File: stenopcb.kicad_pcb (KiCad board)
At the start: 2 copper layers, 97.8 x 97.8 mm, 85 parts, among them K1 MAIN_RIGHT_TO_VOWELS_RIGHT, K2 MAIN_LEFT_TO_VOWELS_LEFT, K3 VOWELS_RIGHT_IN, K4 VOWELS_LEFT_IN, P1 MAIN_RIGHT_IN, P2 MAIN_RIGHT_TO_MAIN_LEFT, P3 MAIN_LEFT_IN, SW1 SPST, SW10 SPST, SW11 SPST, SW12 SPST, SW13 SPST, SW14 SPST, SW15 SPST, SW16 SPST, SW17 SPST, SW18 SPST, SW19 SPST, SW2 SPST, SW20 SPST, SW21 SPST, SW22 SPST, SW23 SPST, SW24 SPST, SW25 SPST, SW26 SPST, SW27 SPST, SW28 SPST, SW29 SPST, SW3 SPST, SW30 SPST, SW4 SPST, SW5 SPST, SW6 SPST, SW7 SPST, SW8 SPST, SW9 SPST

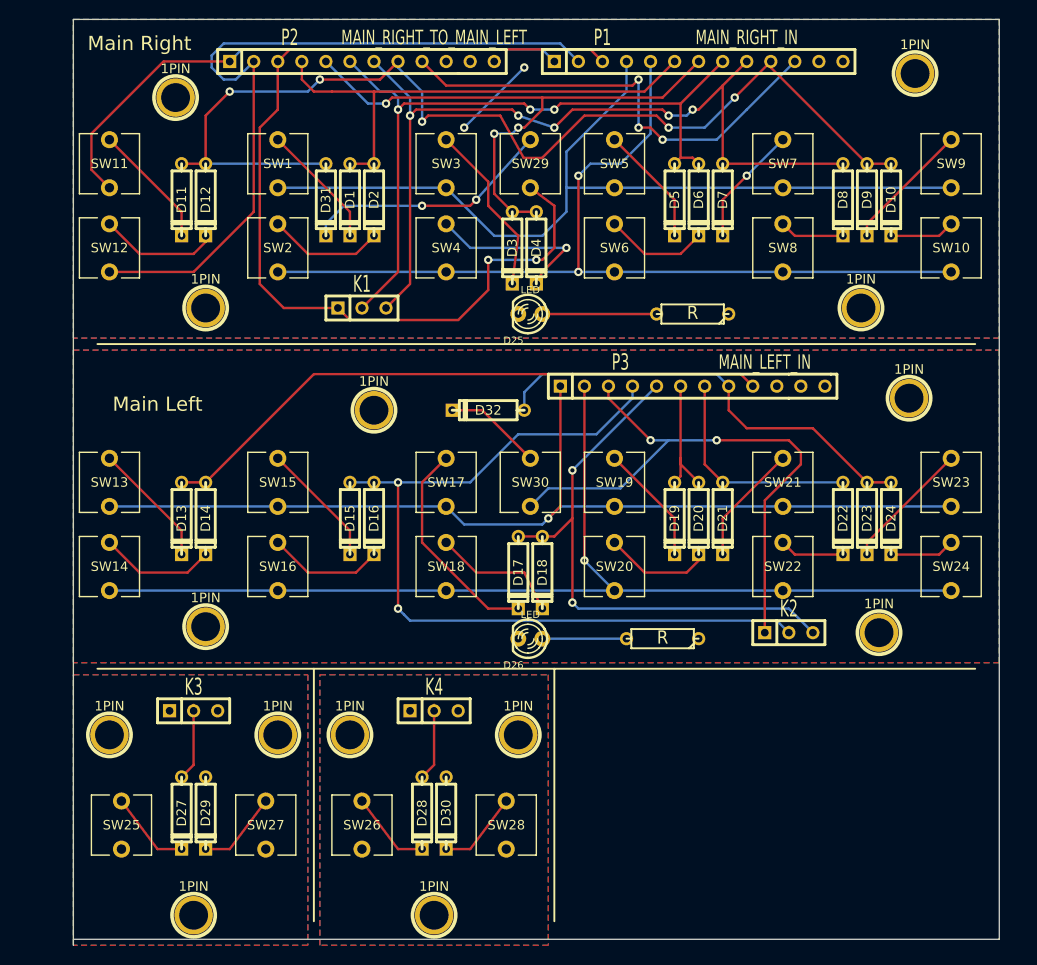
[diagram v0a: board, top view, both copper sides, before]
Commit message: fixed 3-pin connector on main right, and made vowel boards smaller
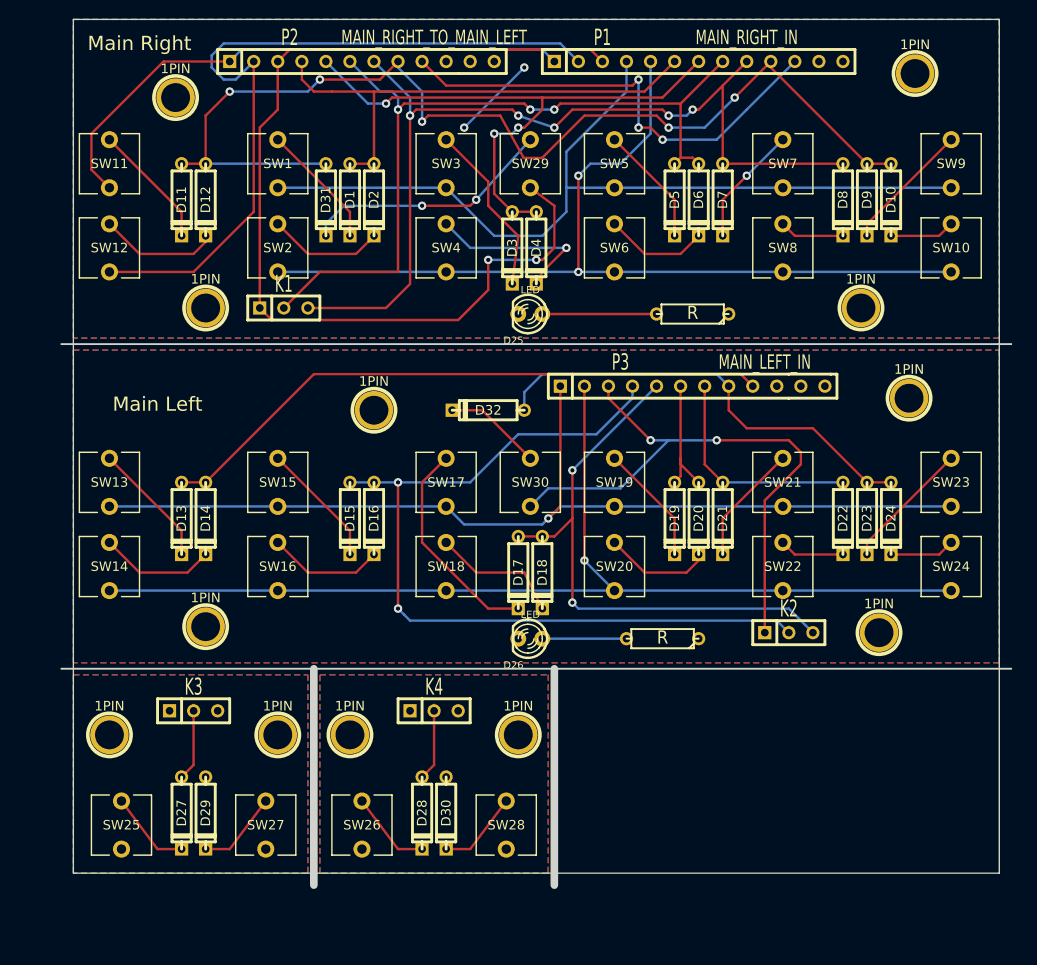
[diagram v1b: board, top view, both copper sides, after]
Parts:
- removed the 1PIN at (123.8, 156.8)
- removed the 1PIN at (149.2, 156.8)
- moved K1 8.25 mm to (133.3, 92.7)
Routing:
- net /COL_3: track 89.3 -> 97.6 mm
- net /COL_2: track 76.2 -> 84.4 mm
- net /ROW_2: track 105.0 -> 106.4 mm
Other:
- board size 97.8 x 97.8 mm -> 100.3 x 91.4 mm
- board text added: "Routing"
- board text added: "V-Scoring"

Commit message: added information text on silkscreen
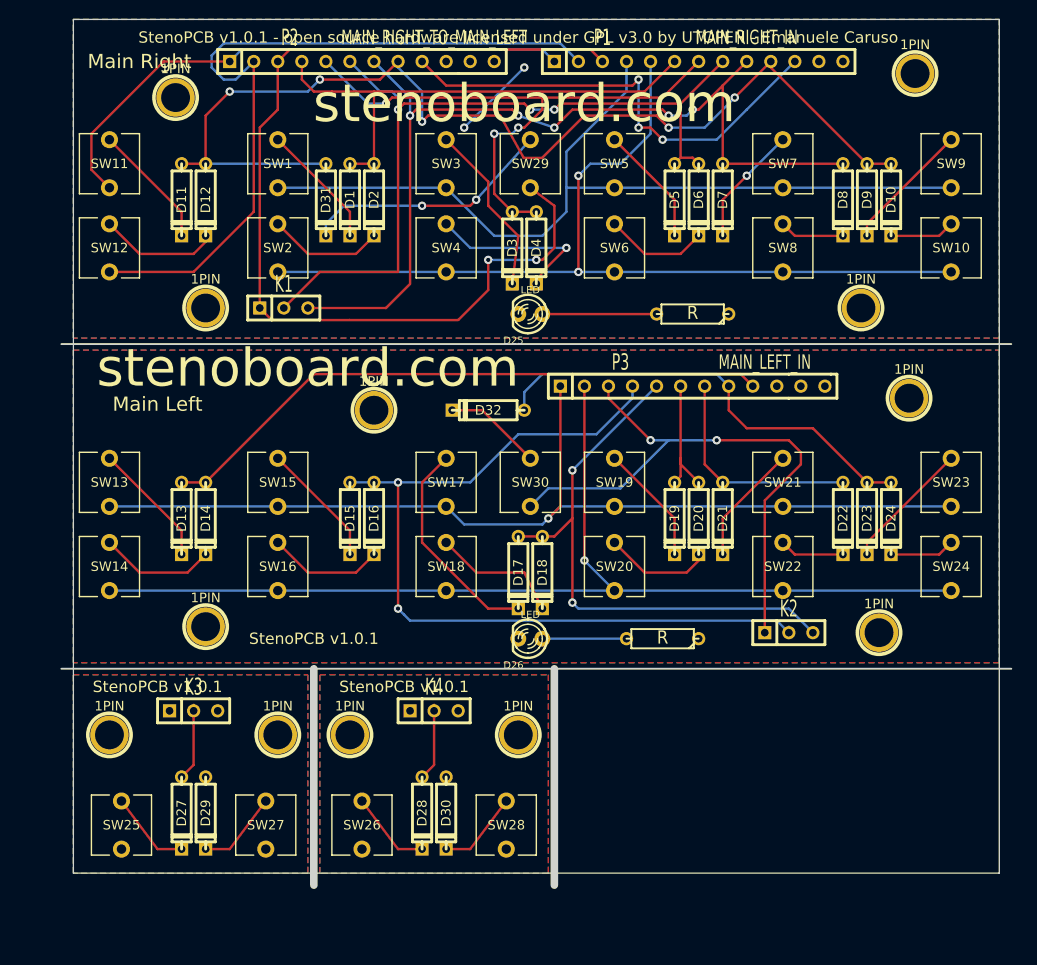
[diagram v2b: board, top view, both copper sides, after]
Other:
- board text added: "StenoPCB v1.0.1"
- board text added: "StenoPCB v1.0.1 - open source hardware licensed under GPL v3.0 by UTOPEN - Emanuele Caruso"
- board text added: "stenoboard.com"
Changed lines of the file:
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@@
     (area 91.694999 45.410001 231.440714 177.325)
     (thickness 1.6)
-    (drawings 36)
+    (drawings 42)
     (tracks 346)
     (zones 0)
@@
     )
   )
+  (gr_text "StenoPCB v1.0.1" (at 120.015 132.715) (layer F.SilkS)
+    (effects (font (size 1.2 1.2) (thickness 0.3)))
+  )
+  (gr_text "StenoPCB v1.0.1" (at 146.05 132.715) (layer F.SilkS)
+    (effects (font (size 1.2 1.2) (thickness 0.3)))
+  )
+  (gr_text "StenoPCB v1.0.1" (at 136.525 127.635) (layer F.SilkS)
+    (effects (font (size 1.2 1.2) (thickness 0.3)))
+  )
+  (gr_text "StenoPCB v1.0.1 - open source hardware licensed under GPL v3.0 by UTOPEN - Emanuele Caruso" (at 158.115 64.135) (layer F.SilkS)
+    (effects (font (size 1.2 1.2) (thickness 0.3)))
+  )
+  (gr_text stenoboard.com (at 135.89 99.06) (layer F.SilkS)
+    (effects (font (size 4 4) (thickness 0.3)))
+  )
+  (gr_text stenoboard.com (at 158.75 71.12) (layer F.SilkS)
+    (effects (font (size 4 4) (thickness 0.3)))
+  )
   (gr_line (start 161.925 130.81) (end 161.925 153.67) (angle 90) (layer Edge.Cuts) (width 0.8))
   (gr_line (start 136.525 130.81) (end 136.525 153.67) (angle 90) (layer Edge.Cuts) (width 0.8))
@@
     (effects (font (size 1.5 1.5) (thickness 0.3)))
   )
-  (gr_text "Main Right" (at 118.11 64.77) (layer F.SilkS)
+  (gr_text "Main Right" (at 118.11 66.675) (layer F.SilkS)
     (effects (font (size 1.5 1.5) (thickness 0.3)))
   )

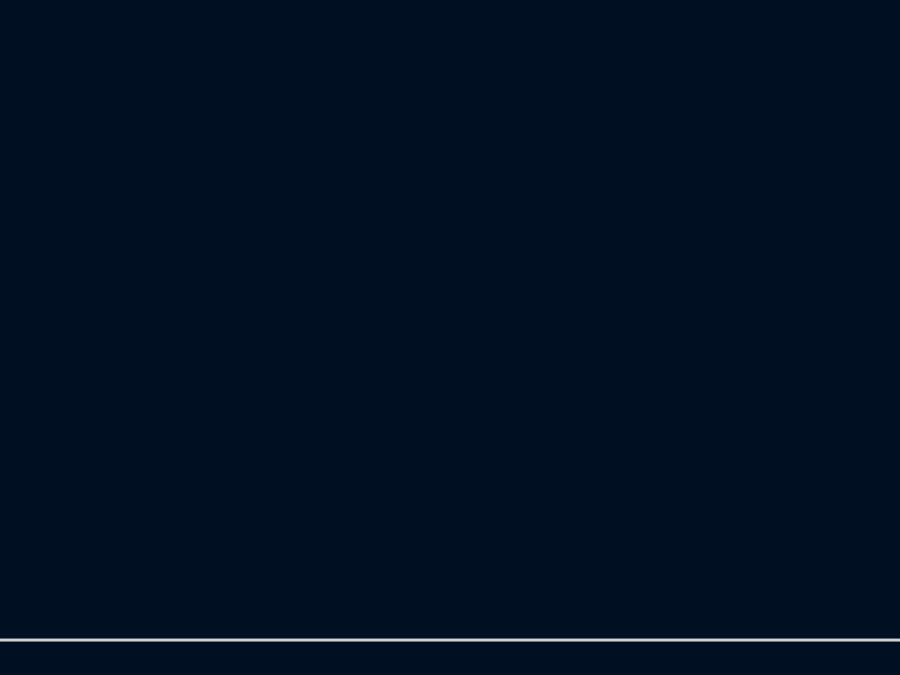
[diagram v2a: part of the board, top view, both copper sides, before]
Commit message: added TOP and BOT copper layers labels
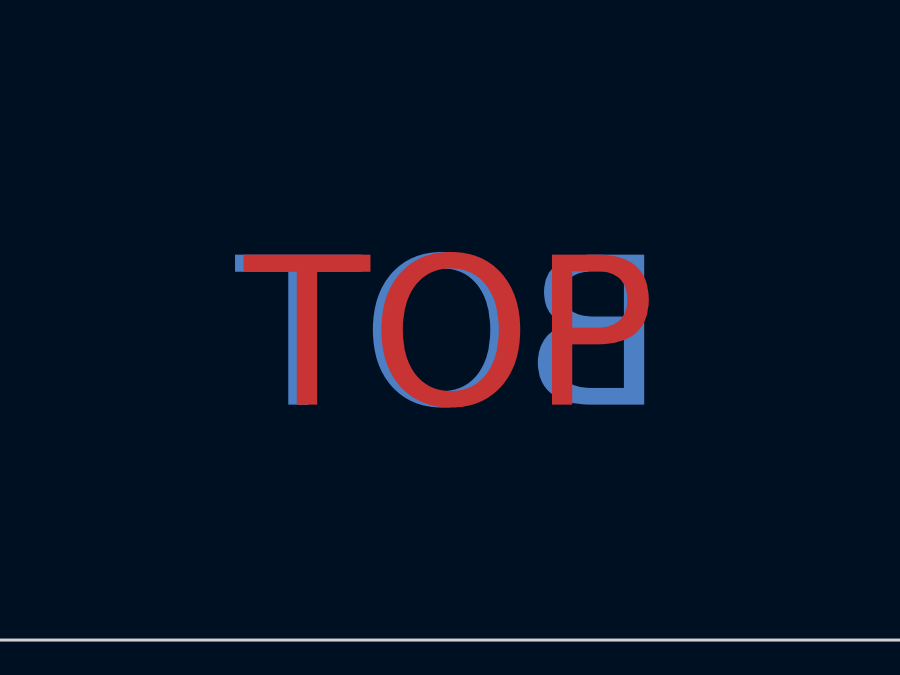
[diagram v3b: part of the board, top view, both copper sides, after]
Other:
- board text added: "BOT"
- board text added: "TOP"
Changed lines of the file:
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@@
     (area 91.694999 45.410001 231.440714 177.325)
     (thickness 1.6)
-    (drawings 42)
+    (drawings 44)
     (tracks 346)
     (zones 0)
@@
     )
   )
+  (gr_text BOT (at 186.055 142.24) (layer B.Cu)
+    (effects (font (size 5 5) (thickness 0.3)) (justify mirror))
+  )
+  (gr_text TOP (at 186.055 142.24) (layer F.Cu)
+    (effects (font (size 5 5) (thickness 0.3)))
+  )
   (gr_text "StenoPCB v1.0.1" (at 120.015 132.715) (layer F.SilkS)

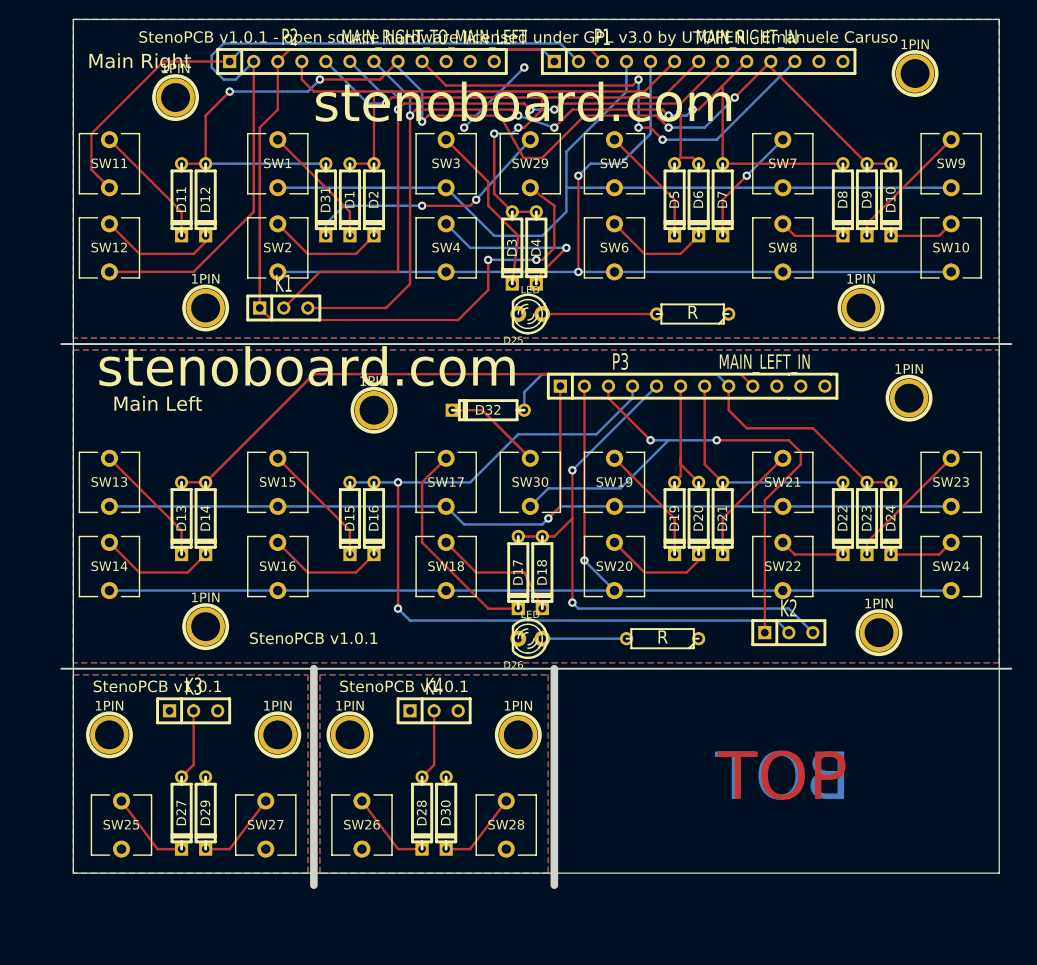
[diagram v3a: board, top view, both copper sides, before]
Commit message: added bottom margin
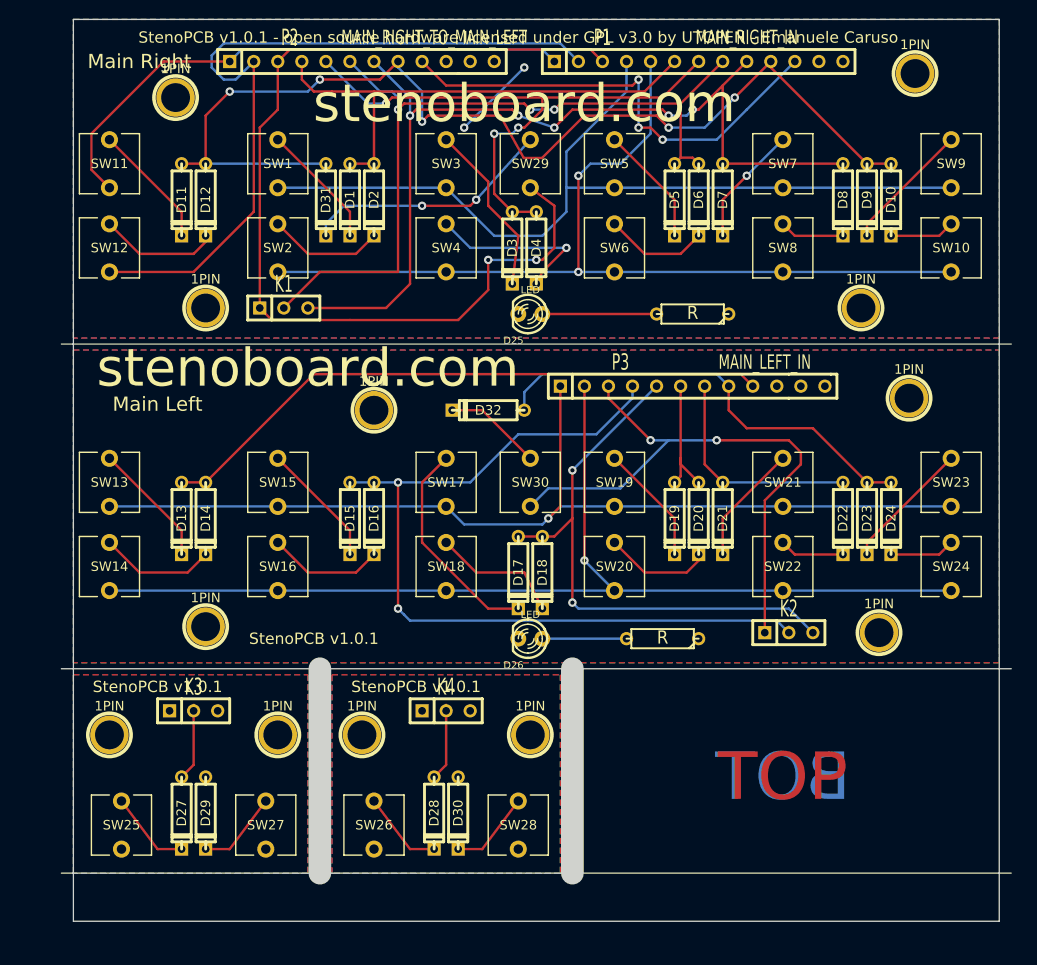
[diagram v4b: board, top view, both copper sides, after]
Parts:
- moved K4 1.27 mm to (150.5, 135.3)
- moved SW26 1.27 mm to (142.9, 147.3)
- moved SW28 1.27 mm to (158.1, 147.3)
- moved 1PIN 1.27 mm to (141.6, 137.8)
- moved 1PIN 1.27 mm to (159.4, 137.8)
- moved D28 1.27 mm to (149.2, 146.1)
- moved D30 1.27 mm to (151.8, 146.1)
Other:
- board size 100.3 x 91.4 mm -> 100.3 x 95.2 mm
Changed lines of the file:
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@@
     (area 91.694999 45.410001 231.440714 177.325)
     (thickness 1.6)
-    (drawings 44)
+    (drawings 48)
     (tracks 346)
     (zones 0)
@@
     (22 B.Mask user)
     (23 F.Mask user)
-    (24 Dwgs.User user)
+    (24 Dwgs.User user hide)
     (25 Cmts.User user)
     (26 Eco1.User user)
@@
   )
   (module SIL-3 (layer F.Cu)
-    (at 149.225 135.255)
+    (at 150.495 135.255)
     (descr "Connecteur 3 pins")
     (tags "CONN DEV")
@@
   )
   (module EVQ-P0E07K (layer F.Cu)
-    (at 156.845 147.32)
+    (at 158.115 147.32)
     (fp_text reference SW28 (at 0 0) (layer F.SilkS)
       (effects (font (size 1 1) (thickness 0.15)))
@@
   )
   (module EVQ-P0E07K (layer F.Cu)
-    (at 141.605 147.32)
+    (at 142.875 147.32)
     (fp_text reference SW26 (at 0 0) (layer F.SilkS)
       (effects (font (size 1 1) (thickness 0.15)))
@@
   )
   (module D3 (layer F.Cu)
-    (at 150.495 146.05 270)
+    (at 151.765 146.05 270)
     (descr "Diode 3 pas")
     (tags "DIODE DEV")
@@
   )
   (module D3 (layer F.Cu)
-    (at 147.955 146.05 270)
+    (at 149.225 146.05 270)
     (descr "Diode 3 pas")
     (tags "DIODE DEV")
@@
   )
   (module 1pin (layer F.Cu)
-    (at 140.335 137.795)
+    (at 141.605 137.795)
     (descr "module 1 pin (ou trou mecanique de percage)")
     (tags DEV)
@@
   )
   (module 1pin (layer F.Cu)
-    (at 158.115 137.795)
+    (at 159.385 137.795)
     (descr "module 1 pin (ou trou mecanique de percage)")
     (tags DEV)
@@
     )
   )
+  (gr_line (start 163.83 130.81) (end 163.83 152.4) (angle 90) (layer Edge.Cuts) (width 2.4))
+  (gr_line (start 137.16 130.81) (end 137.16 152.4) (angle 90) (layer Edge.Cuts) (width 2.4))
+  (gr_text V-Scoring (at 217.17 152.4) (layer Dwgs.User)
+    (effects (font (size 1.5 1.5) (thickness 0.3)))
+  )
+  (gr_line (start 109.855 152.4) (end 210.185 152.4) (angle 90) (layer Edge.Cuts) (width 0.01))
+  (gr_line (start 208.915 157.48) (end 208.915 152.4) (angle 90) (layer Edge.Cuts) (width 0.1))
+  (gr_line (start 111.125 157.48) (end 208.915 157.48) (angle 90) (layer Edge.Cuts) (width 0.1))
+  (gr_line (start 111.125 152.4) (end 111.125 157.48) (angle 90) (layer Edge.Cuts) (width 0.1))
   (gr_text BOT (at 186.055 142.24) (layer B.Cu)
     (effects (font (size 5 5) (thickness 0.3)) (justify mirror))
@@
     (effects (font (size 1.2 1.2) (thickness 0.3)))
   )
-  (gr_text "StenoPCB v1.0.1" (at 146.05 132.715) (layer F.SilkS)
+  (gr_text "StenoPCB v1.0.1" (at 147.32 132.715) (layer F.SilkS)
     (effects (font (size 1.2 1.2) (thickness 0.3)))
   )
@@
     (effects (font (size 4 4) (thickness 0.3)))
   )
-  (gr_line (start 161.925 130.81) (end 161.925 153.67) (angle 90) (layer Edge.Cuts) (width 0.8))
-  (gr_line (start 136.525 130.81) (end 136.525 153.67) (angle 90) (layer Edge.Cuts) (width 0.8))
-  (gr_text Routing (at 166.37 154.94) (layer Dwgs.User)
+  (gr_text Routing (at 167.64 156.21) (layer Dwgs.User)
     (effects (font (size 1.5 1.5) (thickness 0.3)))
   )
-  (gr_text Routing (at 140.97 154.94) (layer Dwgs.User)
+  (gr_text Routing (at 140.97 156.21) (layer Dwgs.User)
     (effects (font (size 1.5 1.5) (thickness 0.3)))
   )
@@
     (arrow2b (pts (xy 99.694998 62.23) (xy 100.281418 63.356503)))
   )
-  (gr_line (start 109.855 130.81) (end 210.185 130.81) (angle 90) (layer Edge.Cuts) (width 0.2))
-  (gr_line (start 109.855 96.52) (end 210.185 96.52) (angle 90) (layer Edge.Cuts) (width 0.2))
+  (gr_line (start 109.855 130.81) (end 210.185 130.81) (angle 90) (layer Edge.Cuts) (width 0.01))
+  (gr_line (start 109.855 96.52) (end 210.185 96.52) (angle 90) (layer Edge.Cuts) (width 0.01))
   (dimension 1.905 (width 0.3) (layer Dwgs.User)
     (gr_text "1,905 mm" (at 174.704999 151.4475 270) (layer Dwgs.User)
@@
   )
   (gr_line (start 111.125 152.4) (end 111.125 62.23) (angle 90) (layer Edge.Cuts) (width 0.1))
-  (gr_line (start 208.915 152.4) (end 111.125 152.4) (angle 90) (layer Edge.Cuts) (width 0.1))
   (gr_line (start 111.125 62.23) (end 208.915 62.23) (angle 90) (layer Edge.Cuts) (width 0.1))
   (via (at 152.4 73.66) (size 0.889) (layers F.Cu B.Cu) (net 0))
@@
   (segment (start 164.465 88.9) (end 168.275 88.9) (width 0.254) (layer B.Cu) (net 24))
   (segment (start 132.715 88.9) (end 150.495 88.9) (width 0.254) (layer B.Cu) (net 24))
-  (segment (start 149.225 134.62) (end 149.225 140.97) (width 0.254) (layer F.Cu) (net 25) (status 10))
-  (segment (start 149.225 140.97) (end 147.955 142.24) (width 0.254) (layer F.Cu) (net 25))
+  (segment (start 150.495 134.62) (end 150.495 140.97) (width 0.254) (layer F.Cu) (net 25) (status 10))
+  (segment (start 150.495 140.97) (end 149.225 142.24) (width 0.254) (layer F.Cu) (net 25))
   (segment (start 123.825 134.62) (end 123.825 140.97) (width 0.254) (layer F.Cu) (net 28) (status 10))
   (segment (start 123.825 140.97) (end 122.555 142.24) (width 0.254) (layer F.Cu) (net 28))
@@
   (segment (start 194.945 118.745) (end 194.945 117.475) (width 0.254) (layer F.Cu) (net 34))
   (segment (start 194.945 117.475) (end 203.835 108.585) (width 0.254) (layer F.Cu) (net 34))
-  (segment (start 147.955 149.86) (end 145.415 149.86) (width 0.254) (layer F.Cu) (net 35))
-  (segment (start 145.415 149.86) (end 141.605 144.78) (width 0.254) (layer F.Cu) (net 35) (status 20))
-  (segment (start 150.495 149.86) (end 153.035 149.86) (width 0.254) (layer F.Cu) (net 36))
-  (segment (start 153.035 149.86) (end 156.845 144.78) (width 0.254) (layer F.Cu) (net 36) (status 20))
+  (segment (start 149.225 149.86) (end 146.685 149.86) (width 0.254) (layer F.Cu) (net 35))
+  (segment (start 146.685 149.86) (end 142.875 144.78) (width 0.254) (layer F.Cu) (net 35) (status 20))
+  (segment (start 151.765 149.86) (end 154.305 149.86) (width 0.254) (layer F.Cu) (net 36))
+  (segment (start 154.305 149.86) (end 158.115 144.78) (width 0.254) (layer F.Cu) (net 36) (status 20))
   (segment (start 122.555 149.86) (end 120.015 149.86) (width 0.254) (layer F.Cu) (net 37))
   (segment (start 120.015 149.86) (end 116.205 144.78) (width 0.254) (layer F.Cu) (net 37) (status 20))
@@
     (polygon
       (pts
-        (xy 161.29 152.4) (xy 137.16 152.4) (xy 137.16 131.445) (xy 161.29 131.445)
+        (xy 162.56 152.4) (xy 138.43 152.4) (xy 138.43 131.445) (xy 162.56 131.445)
       )
     )
@@
     (polygon
       (pts
-        (xy 161.29 152.4) (xy 137.16 152.4) (xy 137.16 131.445) (xy 161.29 131.445)
+        (xy 162.56 152.4) (xy 138.43 152.4) (xy 138.43 131.445) (xy 162.56 131.445)
       )
     )
